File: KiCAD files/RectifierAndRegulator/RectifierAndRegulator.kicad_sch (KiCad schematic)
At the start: 11 parts, among them J1 Input, J2 Output, U1 L7805

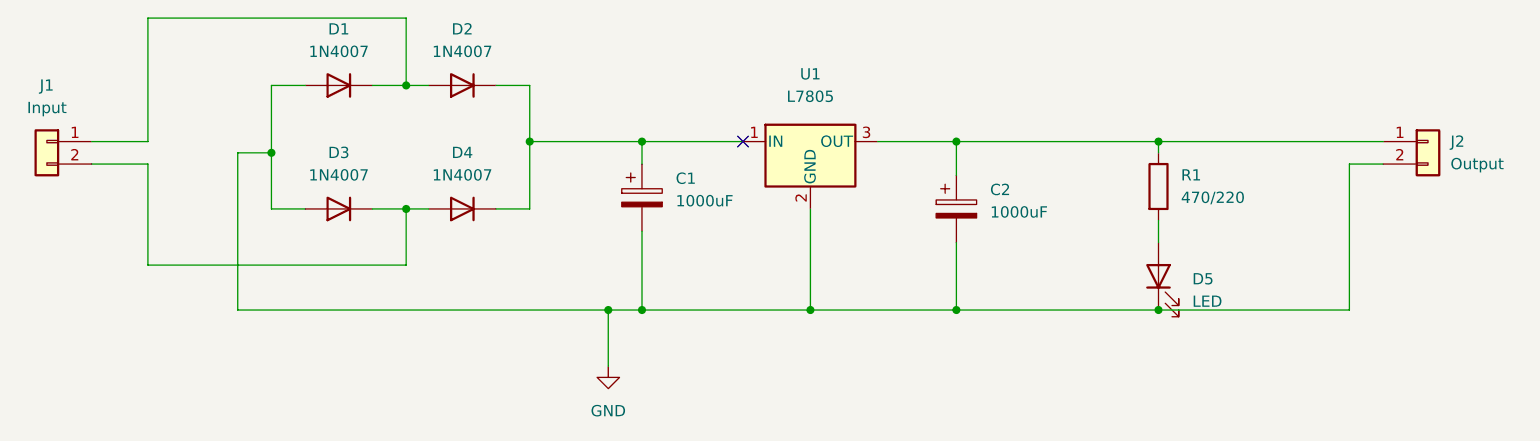
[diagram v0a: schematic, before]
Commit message: Edited Rectifier schematics and PCB
edited the trackwidth from 1mm to 1.5mm
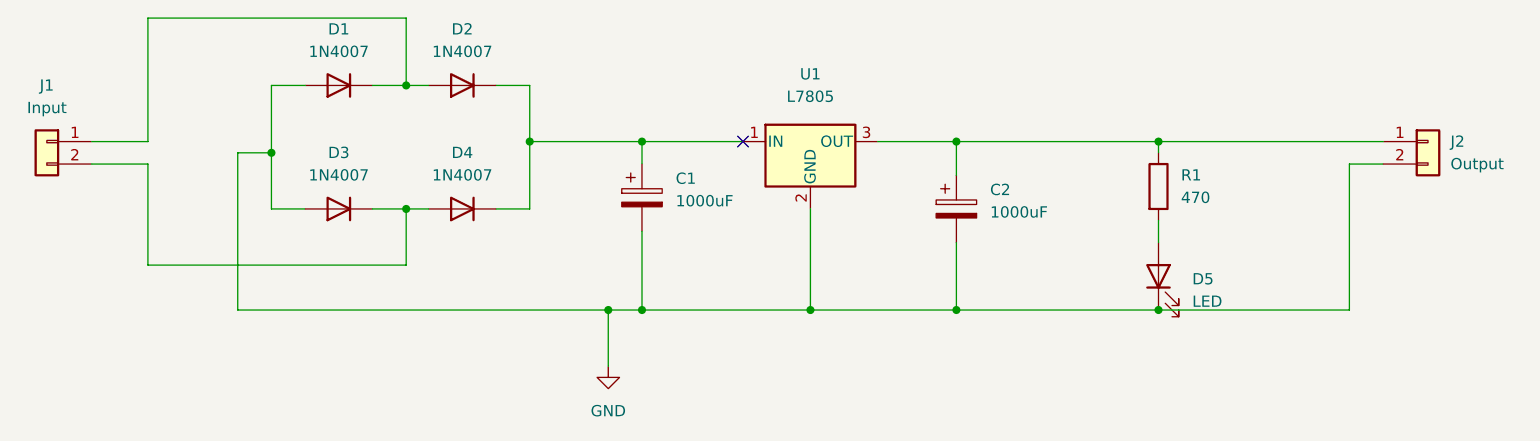
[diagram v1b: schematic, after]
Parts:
- C1, C2: footprint Capacitor_THT:C_Radial_D8.0mm_H7.0mm_P3.50mm -> Capacitor_THT:C_Radial_D10.0mm_H20.0mm_P5.00mm
- R1: value 470/220 -> 470
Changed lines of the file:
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@@
       (effects (font (size 1.27 1.27)) (justify left))
     )
-    (property "Footprint" "Capacitor_THT:C_Radial_D8.0mm_H7.0mm_P3.50mm" (id 2) (at 168.6052 106.68 0)
+    (property "Footprint" "Capacitor_THT:C_Radial_D10.0mm_H20.0mm_P5.00mm" (id 2) (at 168.6052 106.68 0)
       (effects (font (size 1.27 1.27)) hide)
     )
@@
       (effects (font (size 1.27 1.27)) (justify left))
     )
-    (property "Value" "470/220" (id 1) (at 193.04 101.5999 0)
+    (property "Value" "470" (id 1) (at 193.04 101.5999 0)
       (effects (font (size 1.27 1.27)) (justify left))
     )
@@
       (effects (font (size 1.27 1.27)) (justify left))
     )
-    (property "Footprint" "Capacitor_THT:C_Radial_D8.0mm_H7.0mm_P3.50mm" (id 2) (at 133.0452 105.41 0)
+    (property "Footprint" "Capacitor_THT:C_Radial_D10.0mm_H20.0mm_P5.00mm" (id 2) (at 133.0452 105.41 0)
       (effects (font (size 1.27 1.27)) hide)
     )
@@
     )
     (path "/b0d76427-eadd-4494-a4e6-57caeb972e4a"
-      (reference "C1") (unit 1) (value "1000uF") (footprint "Capacitor_THT:C_Radial_D8.0mm_H7.0mm_P3.50mm")
+      (reference "C1") (unit 1) (value "1000uF") (footprint "Capacitor_THT:C_Radial_D10.0mm_H20.0mm_P5.00mm")
     )
     (path "/598fe0fe-299e-48e2-98bb-d0e44f8057ce"
-      (reference "C2") (unit 1) (value "1000uF") (footprint "Capacitor_THT:C_Radial_D8.0mm_H7.0mm_P3.50mm")
+      (reference "C2") (unit 1) (value "1000uF") (footprint "Capacitor_THT:C_Radial_D10.0mm_H20.0mm_P5.00mm")
     )
     (path "/13df134f-9e18-49fd-9099-406b1a7397b3"
@@
     )
     (path "/aa7503f2-df38-4532-bdc5-22a8b9a95d9d"
-      (reference "R1") (unit 1) (value "470/220") (footprint "Resistor_THT:R_Axial_DIN0207_L6.3mm_D2.5mm_P10.16mm_Horizontal")
+      (reference "R1") (unit 1) (value "470") (footprint "Resistor_THT:R_Axial_DIN0207_L6.3mm_D2.5mm_P10.16mm_Horizontal")
     )
     (path "/a1a1507a-b7ba-4169-b299-e0bb041a1cb6"

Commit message: edited oops
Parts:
- C1, C2: value 1000uF -> (none)
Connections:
- no-connect marks 1 -> 0
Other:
- moved on the sheet: C1, C2, D1, D2, D3, D4, D5, J1, J2, R1

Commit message: halka edit smoothing capacitor ma
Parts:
- added C2: (no value), Capacitor_THT:CP_Radial_D6.3mm_P2.50mm, symbol Device:C_Polarized
- C1: footprint Capacitor_THT:C_Radial_D10.0mm_H20.0mm_P5.00mm -> Capacitor_THT:CP_Radial_D8.0mm_P2.50mm
- C3: renamed from C2; footprint Capacitor_THT:C_Radial_D10.0mm_H20.0mm_P5.00mm -> Capacitor_THT:CP_Radial_D5.0mm_P2.50mm
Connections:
- net GND: now also C2.2
- net at C1.1, D2.1 (K), D4.1 (K)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: now also C2.1
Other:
- moved on the sheet: U1
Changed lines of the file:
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@@
   (junction (at 163.83 95.25) (diameter 0) (color 0 0 0 0)
   )
+  (junction (at 146.05 114.3) (diameter 0) (color 0 0 0 0)
+  )
   (junction (at 176.53 95.25) (diameter 0) (color 0 0 0 0)
   )
+  (junction (at 146.05 95.25) (diameter 0) (color 0 0 0 0)
+  )
   (junction (at 119.38 88.9) (diameter 0) (color 0 0 0 0)
   )
-  (junction (at 151.13 114.3) (diameter 0) (color 0 0 0 0)
+  (junction (at 154.94 114.3) (diameter 0) (color 0 0 0 0)
   )
   (junction (at 104.14 96.52) (diameter 0) (color 0 0 0 0)
@@
     (stroke (width 0) (type default) (color 0 0 0 0))
   )
+  (wire (pts (xy 146.05 95.25) (xy 146.05 97.79))
+    (stroke (width 0) (type default) (color 0 0 0 0))
+  )
   (wire (pts (xy 176.53 95.25) (xy 190.5 95.25))
     (stroke (width 0) (type default) (color 0 0 0 0))
@@
     (stroke (width 0) (type default) (color 0 0 0 0))
   )
+  (wire (pts (xy 146.05 95.25) (xy 147.32 95.25))
+    (stroke (width 0) (type default) (color 0 0 0 0))
+  )
   (wire (pts (xy 115.57 88.9) (xy 119.38 88.9))
     (stroke (width 0) (type default) (color 0 0 0 0))
@@
     (stroke (width 0) (type default) (color 0 0 0 0))
   )
-  (wire (pts (xy 149.86 114.3) (xy 139.7 114.3))
+  (wire (pts (xy 149.86 114.3) (xy 146.05 114.3))
     (stroke (width 0) (type default) (color 0 0 0 0))
   )
@@
     (stroke (width 0) (type default) (color 0 0 0 0))
   )
-  (wire (pts (xy 139.7 95.25) (xy 143.51 95.25))
+  (wire (pts (xy 146.05 105.41) (xy 146.05 114.3))
+    (stroke (width 0) (type default) (color 0 0 0 0))
+  )
+  (wire (pts (xy 139.7 95.25) (xy 146.05 95.25))
     (stroke (width 0) (type default) (color 0 0 0 0))
   )
@@
     (stroke (width 0) (type default) (color 0 0 0 0))
   )
-  (wire (pts (xy 149.86 114.3) (xy 151.13 114.3))
+  (wire (pts (xy 149.86 114.3) (xy 154.94 114.3))
     (stroke (width 0) (type default) (color 0 0 0 0))
   )
@@
     (stroke (width 0) (type default) (color 0 0 0 0))
   )
-  (wire (pts (xy 151.13 114.3) (xy 163.83 114.3))
-    (stroke (width 0) (type default) (color 0 0 0 0))
-  )
-  (wire (pts (xy 151.13 102.87) (xy 151.13 114.3))
+  (wire (pts (xy 146.05 114.3) (xy 139.7 114.3))
+    (stroke (width 0) (type default) (color 0 0 0 0))
+  )
+  (wire (pts (xy 154.94 114.3) (xy 163.83 114.3))
+    (stroke (width 0) (type default) (color 0 0 0 0))
+  )
+  (wire (pts (xy 154.94 102.87) (xy 154.94 114.3))
     (stroke (width 0) (type default) (color 0 0 0 0))
   )
@@
     (stroke (width 0) (type default) (color 0 0 0 0))
   )
-  (wire (pts (xy 158.75 95.25) (xy 163.83 95.25))
+  (wire (pts (xy 162.56 95.25) (xy 163.83 95.25))
     (stroke (width 0) (type default) (color 0 0 0 0))
   )
@@
     (pin "2")
   )
+  (symbol (lib_id "Device:C_Polarized") (at 146.05 101.6 0) (unit 1)
+    (in_bom yes) (on_board yes) (fields_autoplaced)
+    (property "Reference" "C2" (id 0) (at 149.86 99.4409 0)
+      (effects (font (size 1.27 1.27)) (justify left))
+    )
+    (property "Value" " " (id 1) (at 149.86 101.9809 0)
+      (effects (font (size 1.27 1.27)) (justify left))
+    )
+    (property "Footprint" "Capacitor_THT:CP_Radial_D6.3mm_P2.50mm" (id 2) (at 147.0152 105.41 0)
+      (effects (font (size 1.27 1.27)) hide)
+    )
+    (property "Datasheet" "~" (id 3) (at 146.05 101.6 0)
+      (effects (font (size 1.27 1.27)) hide)
+    )
+    (pin "1")
+    (pin "2")
+  )
   (symbol (lib_id "Device:C_Polarized") (at 163.83 102.87 0) (unit 1)
     (in_bom yes) (on_board yes) (fields_autoplaced)
-    (property "Reference" "C2" (id 0) (at 167.64 100.7109 0)
+    (property "Reference" "C3" (id 0) (at 167.64 100.7109 0)
       (effects (font (size 1.27 1.27)) (justify left))
     )
@@
       (effects (font (size 1.27 1.27)) (justify left))
     )
-    (property "Footprint" "Capacitor_THT:C_Radial_D10.0mm_H20.0mm_P5.00mm" (id 2) (at 164.7952 106.68 0)
+    (property "Footprint" "Capacitor_THT:CP_Radial_D5.0mm_P2.50mm" (id 2) (at 164.7952 106.68 0)
       (effects (font (size 1.27 1.27)) hide)
     )
@@
     (pin "2")
   )
-  (symbol (lib_id "Regulator_Linear:L7805") (at 151.13 95.25 0) (unit 1)
-    (in_bom yes) (on_board yes) (fields_autoplaced)
-    (property "Reference" "U1" (id 0) (at 151.13 87.63 0))
-    (property "Value" "L7805" (id 1) (at 151.13 90.17 0))
-    (property "Footprint" "Connector_PinSocket_2.54mm:PinSocket_1x03_P2.54mm_Vertical" (id 2) (at 151.765 99.06 0)
+  (symbol (lib_id "Regulator_Linear:L7805") (at 154.94 95.25 0) (unit 1)
+    (in_bom yes) (on_board yes) (fields_autoplaced)
+    (property "Reference" "U1" (id 0) (at 154.94 87.63 0))
+    (property "Value" "L7805" (id 1) (at 154.94 90.17 0))
+    (property "Footprint" "Connector_PinSocket_2.54mm:PinSocket_1x03_P2.54mm_Vertical" (id 2) (at 155.575 99.06 0)
       (effects (font (size 1.27 1.27) italic) (justify left) hide)
     )
-    (property "Datasheet" "http://www.st.com/content/ccc/resource/technical/document/datasheet/41/4f/b3/b0/12/d4/47/88/CD00000444.pdf/files/CD00000444.pdf/jcr:content/translations/en.CD00000444.pdf" (id 3) (at 151.13 96.52 0)
+    (property "Datasheet" "http://www.st.com/content/ccc/resource/technical/document/datasheet/41/4f/b3/b0/12/d4/47/88/CD00000444.pdf/files/CD00000444.pdf/jcr:content/translations/en.CD00000444.pdf" (id 3) (at 154.94 96.52 0)
       (effects (font (size 1.27 1.27)) hide)
     )
@@
       (effects (font (size 1.27 1.27)) (justify left))
     )
-    (property "Footprint" "Capacitor_THT:C_Radial_D10.0mm_H20.0mm_P5.00mm" (id 2) (at 140.6652 105.41 0)
+    (property "Footprint" "Capacitor_THT:CP_Radial_D8.0mm_P2.50mm" (id 2) (at 140.6652 105.41 0)
       (effects (font (size 1.27 1.27)) hide)
     )
@@
     )
     (path "/b0d76427-eadd-4494-a4e6-57caeb972e4a"
-      (reference "C1") (unit 1) (value " ") (footprint "Capacitor_THT:C_Radial_D10.0mm_H20.0mm_P5.00mm")
+      (reference "C1") (unit 1) (value " ") (footprint "Capacitor_THT:CP_Radial_D8.0mm_P2.50mm")
+    )
+    (path "/19906e76-bf3a-48d4-9765-5125c13e02c2"
+      (reference "C2") (unit 1) (value " ") (footprint "Capacitor_THT:CP_Radial_D6.3mm_P2.50mm")
     )
     (path "/598fe0fe-299e-48e2-98bb-d0e44f8057ce"
-      (reference "C2") (unit 1) (value " ") (footprint "Capacitor_THT:C_Radial_D10.0mm_H20.0mm_P5.00mm")
+      (reference "C3") (unit 1) (value " ") (footprint "Capacitor_THT:CP_Radial_D5.0mm_P2.50mm")
     )
     (path "/13df134f-9e18-49fd-9099-406b1a7397b3"

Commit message: edited size of capacitor footprint
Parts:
- C1: footprint Capacitor_THT:CP_Radial_D8.0mm_P2.50mm -> Capacitor_THT:CP_Radial_D10.0mm_P5.00mm
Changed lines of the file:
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@@
       (effects (font (size 1.27 1.27)) (justify left))
     )
-    (property "Footprint" "Capacitor_THT:CP_Radial_D8.0mm_P2.50mm" (id 2) (at 140.6652 105.41 0)
+    (property "Footprint" "Capacitor_THT:CP_Radial_D10.0mm_P5.00mm" (id 2) (at 140.6652 105.41 0)
       (effects (font (size 1.27 1.27)) hide)
     )
@@
     )
     (path "/b0d76427-eadd-4494-a4e6-57caeb972e4a"
-      (reference "C1") (unit 1) (value " ") (footprint "Capacitor_THT:CP_Radial_D8.0mm_P2.50mm")
+      (reference "C1") (unit 1) (value " ") (footprint "Capacitor_THT:CP_Radial_D10.0mm_P5.00mm")
     )
     (path "/19906e76-bf3a-48d4-9765-5125c13e02c2"
